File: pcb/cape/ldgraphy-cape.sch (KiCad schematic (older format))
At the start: 26 parts, among them J1 CONN_01X03, P2 PhDiode, P3 Jumper, P4 BaseConn, P5 CONN_01X05, P6 12V-in, P9 BB_P9, U1 POLOLUSTEPPER, U2 DCDC1584, U3 MIC920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

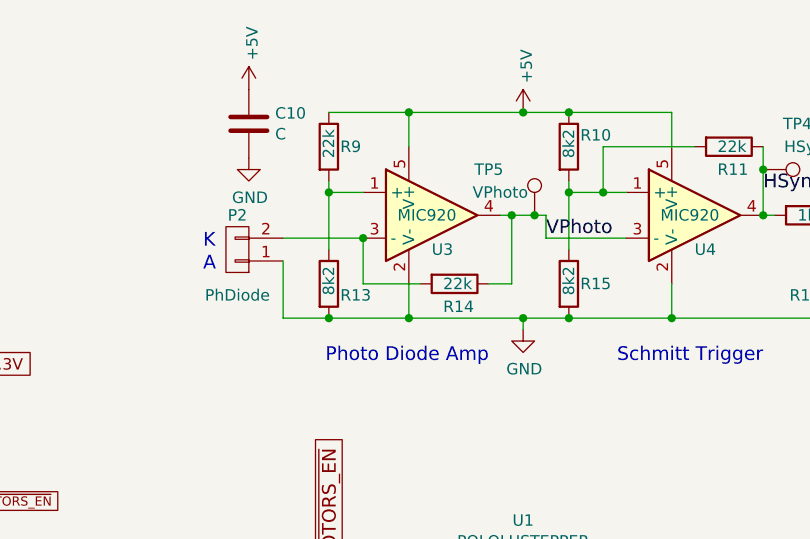
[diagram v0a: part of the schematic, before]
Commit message: Add photo diode compensating cap in feedback loop.
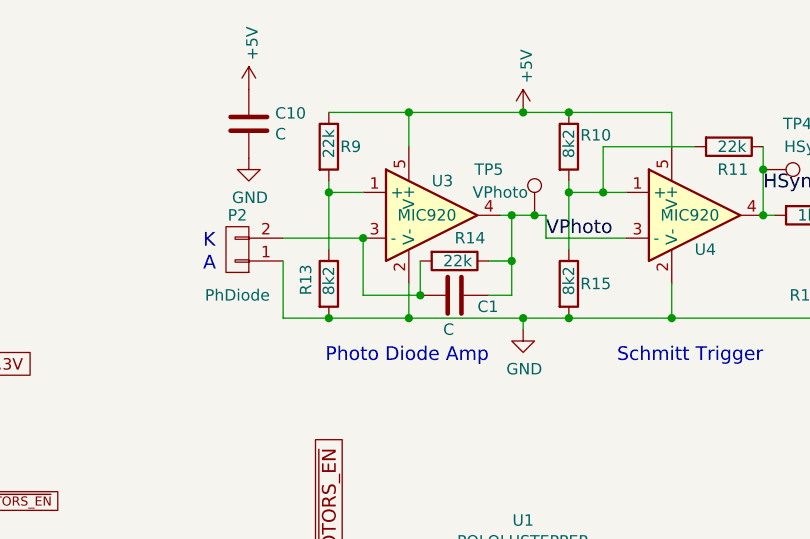
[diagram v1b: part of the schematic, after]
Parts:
- added C1: C, Capacitors_SMD:C_0603, symbol C
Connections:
- net VPhoto: now also C1.1
- net at P2.2 (P2), R14.2, U3.3 (-): now also C1.2
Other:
- moved on the sheet: R14
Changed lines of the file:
@@
 $EndDescr
 $Comp
-L GND #PWR1
+L GND #PWR01
 U 1 1 58730E5F
 P 2550 2200
-F 0 "#PWR1" H 2550 1950 50  0001 C CNN
+F 0 "#PWR01" H 2550 1950 50  0001 C CNN
 F 1 "GND" V 2555 2072 50  0000 R CNN
 F 2 "" H 2550 2200 50  0000 C CNN
@@
 $EndComp
 $Comp
-L GND #PWR2
+L GND #PWR02
 U 1 1 58730E7E
 P 3250 2200
-F 0 "#PWR2" H 3250 1950 50  0001 C CNN
+F 0 "#PWR02" H 3250 1950 50  0001 C CNN
 F 1 "GND" V 3255 2072 50  0000 R CNN
 F 2 "" H 3250 2200 50  0000 C CNN
@@
 ~MOTORS_EN
 $Comp
-L +12V #PWR9
+L +12V #PWR09
 U 1 1 58731DA0
 P 6900 3300
-F 0 "#PWR9" H 6900 3150 50  0001 C CNN
+F 0 "#PWR09" H 6900 3150 50  0001 C CNN
 F 1 "+12V" H 6915 3473 50  0000 C CNN
 F 2 "" H 6900 3300 50  0000 C CNN
@@
 $EndComp
 $Comp
-L GND #PWR10
+L GND #PWR010
 U 1 1 587320E9
 P 6950 3450
-F 0 "#PWR10" H 6950 3200 50  0001 C CNN
+F 0 "#PWR010" H 6950 3200 50  0001 C CNN
 F 1 "GND" V 6955 3322 50  0000 R CNN
 F 2 "" H 6950 3450 50  0000 C CNN
@@
 3.3V
 $Comp
-L GND #PWR15
+L GND #PWR015
 U 1 1 587334B3
 P 6900 4050
-F 0 "#PWR15" H 6900 3800 50  0001 C CNN
+F 0 "#PWR015" H 6900 3800 50  0001 C CNN
 F 1 "GND" H 6905 3877 50  0000 C CNN
 F 2 "" H 6900 4050 50  0000 C CNN
@@
 $EndComp
 $Comp
-L +12V #PWR19
+L +12V #PWR019
 U 1 1 58736DA2
 P 2600 5250
-F 0 "#PWR19" H 2600 5100 50  0001 C CNN
+F 0 "#PWR019" H 2600 5100 50  0001 C CNN
 F 1 "+12V" V 2615 5378 50  0000 L CNN
 F 2 "" H 2600 5250 50  0000 C CNN
@@
 MIRROR_CLK
 $Comp
-L GND #PWR18
+L GND #PWR018
 U 1 1 58738059
 P 2550 5150
-F 0 "#PWR18" H 2550 4900 50  0001 C CNN
+F 0 "#PWR018" H 2550 4900 50  0001 C CNN
 F 1 "GND" V 2555 5022 50  0000 R CNN
 F 2 "" H 2550 5150 50  0000 C CNN
@@
 $EndComp
 $Comp
-L GND #PWR17
+L GND #PWR017
 U 1 1 587405F8
 P 2100 1600
-F 0 "#PWR17" H 2100 1350 50  0001 C CNN
+F 0 "#PWR017" H 2100 1350 50  0001 C CNN
 F 1 "GND" H 2105 1427 50  0000 C CNN
 F 2 "" H 2100 1600 50  0000 C CNN
@@
 $EndComp
 $Comp
-L +12V #PWR13
+L +12V #PWR013
 U 1 1 5874068D
 P 2300 1250
-F 0 "#PWR13" H 2300 1100 50  0001 C CNN
+F 0 "#PWR013" H 2300 1100 50  0001 C CNN
 F 1 "+12V" H 2315 1423 50  0000 C CNN
 F 2 "" H 2300 1250 50  0000 C CNN
@@
 $EndComp
 $Comp
-L PWR_FLAG #FLG1
+L PWR_FLAG #FLG01
 U 1 1 587406CB
 P 2300 1250
-F 0 "#FLG1" H 2300 1345 50  0001 C CNN
+F 0 "#FLG01" H 2300 1345 50  0001 C CNN
 F 1 "PWR_FLAG" H 2300 1300 50  0000 C CNN
 F 2 "" H 2300 1250 50  0000 C CNN
@@
 $EndComp
 $Comp
-L +5V #PWR5
+L +5V #PWR05
 U 1 1 58741152
 P 3150 2400
-F 0 "#PWR5" H 3150 2250 50  0001 C CNN
+F 0 "#PWR05" H 3150 2250 50  0001 C CNN
 F 1 "+5V" V 3165 2528 50  0000 L CNN
 F 2 "" H 3150 2400 50  0000 C CNN
@@
 $EndComp
 $Comp
-L +5V #PWR4
+L +5V #PWR04
 U 1 1 587412CA
 P 2650 2400
-F 0 "#PWR4" H 2650 2250 50  0001 C CNN
+F 0 "#PWR04" H 2650 2250 50  0001 C CNN
 F 1 "+5V" V 2665 2528 50  0000 L CNN
 F 2 "" H 2650 2400 50  0000 C CNN
@@
 $EndComp
 $Comp
-L GND #PWR11
+L GND #PWR011
 U 1 1 58D57083
 P 7750 3450
-F 0 "#PWR11" H 7750 3200 50  0001 C CNN
+F 0 "#PWR011" H 7750 3200 50  0001 C CNN
 F 1 "GND" V 7755 3322 50  0000 R CNN
 F 2 "" H 7750 3450 50  0000 C CNN
@@
 $EndComp
 $Comp
-L GND #PWR12
+L GND #PWR012
 U 1 1 58D57138
 P 7750 3950
-F 0 "#PWR12" H 7750 3700 50  0001 C CNN
+F 0 "#PWR012" H 7750 3700 50  0001 C CNN
 F 1 "GND" V 7755 3822 50  0000 R CNN
 F 2 "" H 7750 3950 50  0000 C CNN
@@
 $EndComp
 $Comp
-L MIC920 U3
-U 1 1 58D6A8C4
-P 5750 1650
-F 0 "U3" H 5750 1500 50  0000 L CNN
-F 1 "MIC920" H 5600 1650 50  0000 L CNN
-F 2 "TO_SOT_Packages_SMD:SOT-353_SC-70-5" H 5700 1750 50  0001 C CNN
-F 3 "" H 5800 1850 50  0000 C CNN
-	1    5750 1650
-	1    0    0    -1
-$EndComp
-$Comp
-L GND #PWR8
+L GND #PWR08
 U 1 1 58D6A8CA
 P 6150 2150
-F 0 "#PWR8" H 6150 1900 50  0001 C CNN
+F 0 "#PWR08" H 6150 1900 50  0001 C CNN
 F 1 "GND" H 6155 1977 50  0000 C CNN
 F 2 "" H 6150 2150 50  0000 C CNN
@@
 $EndComp
 $Comp
-L +5V #PWR6
+L +5V #PWR06
 U 1 1 58D6A8D0
 P 6150 1200
-F 0 "#PWR6" H 6150 1050 50  0001 C CNN
+F 0 "#PWR06" H 6150 1050 50  0001 C CNN
 F 1 "+5V" V 6165 1328 50  0000 L CNN
 F 2 "" H 6150 1200 50  0000 C CNN
@@
 U 1 1 58D6CFC4
 P 5300 1950
-F 0 "R13" H 5350 1900 50  0000 L CNN
+F 0 "R13" V 5200 1900 50  0000 L CNN
 F 1 "8k2" V 5300 1900 50  0000 L CNN
 F 2 "Resistors_SMD:R_0603" V 5230 1950 50  0001 C CNN
@@
 L R R14
 U 1 1 58D71CF4
-P 5850 1950
-F 0 "R14" V 5950 1900 50  0000 L CNN
-F 1 "22k" V 5850 1900 50  0000 L CNN
-F 2 "Resistors_SMD:R_0603" V 5780 1950 50  0001 C CNN
-F 3 "" H 5850 1950 50  0000 C CNN
-	1    5850 1950
+P 5850 1850
+F 0 "R14" V 5750 1850 50  0000 L CNN
+F 1 "22k" V 5850 1800 50  0000 L CNN
+F 2 "Resistors_SMD:R_0603" V 5780 1850 50  0001 C CNN
+F 3 "" H 5850 1850 50  0000 C CNN
+	1    5850 1850
 	0    1    1    0
 $EndComp
@@
 	5650 1200 5650 1350
 Wire Wire Line
-	5450 1750 5450 1950
-Wire Wire Line
-	5450 1950 5700 1950
-Wire Wire Line
-	6000 1950 6100 1950
-Wire Wire Line
-	6100 1950 6100 1650
+	6100 1650 6100 2000
 Connection ~ 6100 1650
 Wire Wire Line
@@
 $EndComp
 $Comp
-L +5V #PWR3
+L +5V #PWR03
 U 1 1 58D78329
 P 4950 1100
-F 0 "#PWR3" H 4950 950 50  0001 C CNN
+F 0 "#PWR03" H 4950 950 50  0001 C CNN
 F 1 "+5V" V 4965 1228 50  0000 L CNN
 F 2 "" H 4950 1100 50  0000 C CNN
@@
 $EndComp
 $Comp
-L GND #PWR7
+L GND #PWR07
 U 1 1 58D78392
 P 4950 1400
-F 0 "#PWR7" H 4950 1150 50  0001 C CNN
+F 0 "#PWR07" H 4950 1150 50  0001 C CNN
 F 1 "GND" H 4955 1227 50  0000 C CNN
 F 2 "" H 4950 1400 50  0000 C CNN
@@
 LASER_DATA
 $Comp
-L +12V #PWR20
+L +12V #PWR020
 U 1 1 58E428C1
 P 2700 5700
-F 0 "#PWR20" H 2700 5550 50  0001 C CNN
+F 0 "#PWR020" H 2700 5550 50  0001 C CNN
 F 1 "+12V" V 2715 5828 50  0000 L CNN
 F 2 "" H 2700 5700 50  0000 C CNN
@@
 $EndComp
 $Comp
-L GND #PWR21
+L GND #PWR021
 U 1 1 58E4291D
 P 2700 5900
-F 0 "#PWR21" H 2700 5650 50  0001 C CNN
+F 0 "#PWR021" H 2700 5650 50  0001 C CNN
 F 1 "GND" V 2705 5772 50  0000 R CNN
 F 2 "" H 2700 5900 50  0000 C CNN
@@
 Connection ~ 2100 1450
 $Comp
-L +5V #PWR14
+L +5V #PWR014
 U 1 1 58E9A265
 P 3700 1250
-F 0 "#PWR14" H 3700 1100 50  0001 C CNN
+F 0 "#PWR014" H 3700 1100 50  0001 C CNN
 F 1 "+5V" V 3715 1378 50  0000 L CNN
 F 2 "" H 3700 1250 50  0000 C CNN
@@
 $EndComp
 $Comp
-L GND #PWR16
+L GND #PWR016
 U 1 1 58E9A4E0
 P 3700 1450
-F 0 "#PWR16" H 3700 1200 50  0001 C CNN
+F 0 "#PWR016" H 3700 1200 50  0001 C CNN
 F 1 "GND" H 3705 1277 50  0000 C CNN
 F 2 "" H 3700 1450 50  0000 C CNN
@@
 	1    0    0    -1
 $EndComp
+$Comp
+L C C1
+U 1 1 59B5393C
+P 5850 2000
+F 0 "C1" V 5900 2100 50  0000 L CNN
+F 1 "C" V 6000 1950 50  0000 L CNN
+F 2 "Capacitors_SMD:C_0603" H 5965 1909 50  0001 L CNN
+F 3 "" H 5850 2000 50  0000 C CNN
+	1    5850 2000
+	0    1    1    0
+$EndComp
+Wire Wire Line
+	6000 1850 6100 1850
+Connection ~ 6100 1850
+$Comp
+L MIC920 U3
+U 1 1 58D6A8C4
+P 5750 1650
+F 0 "U3" H 5750 1800 50  0000 L CNN
+F 1 "MIC920" H 5600 1650 50  0000 L CNN
+F 2 "TO_SOT_Packages_SMD:SOT-353_SC-70-5" H 5700 1750 50  0001 C CNN
+F 3 "" H 5800 1850 50  0000 C CNN
+	1    5750 1650
+	1    0    0    -1
+$EndComp
+Wire Wire Line
+	5450 1750 5450 2000
+Wire Wire Line
+	5450 2000 5700 2000
+Wire Wire Line
+	6100 2000 6000 2000
+Wire Wire Line
+	5700 2000 5700 1850
+Connection ~ 5700 2000
 $EndSCHEMATC
